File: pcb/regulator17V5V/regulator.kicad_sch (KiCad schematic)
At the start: 8 parts, among them J1 Conn_01x05_Socket, J2 Conn_01x05_Socket, J3 Conn_01x02, U1 TPS82130

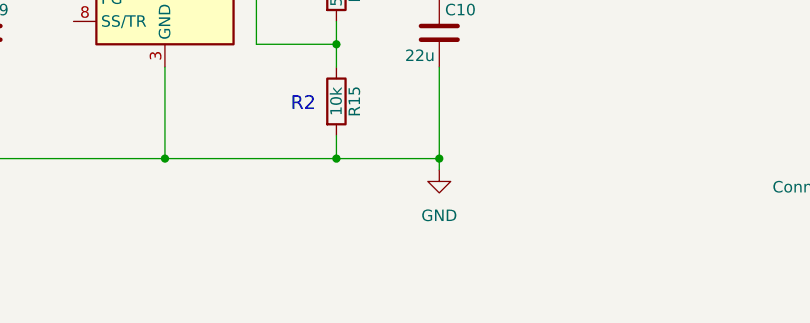
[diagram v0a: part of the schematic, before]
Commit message: Add receiver for IKEA Metod cupboard
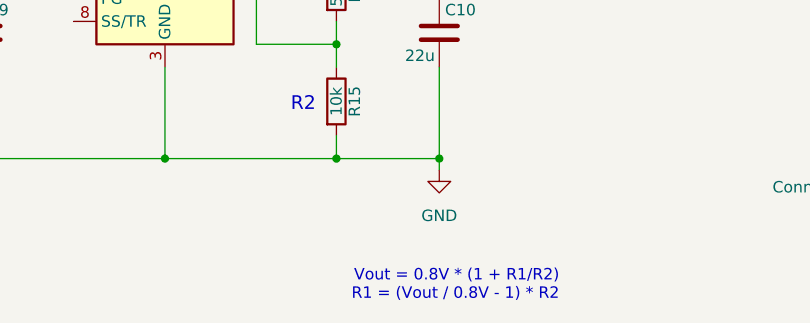
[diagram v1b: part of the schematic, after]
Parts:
- J1, J2: footprint local:Holes -> local:SolderHoles3pin10mm
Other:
- note added: "Vout = 0.8V * (1 + R1/R2) R1 = (Vout / 0.8V - 1) * R2"

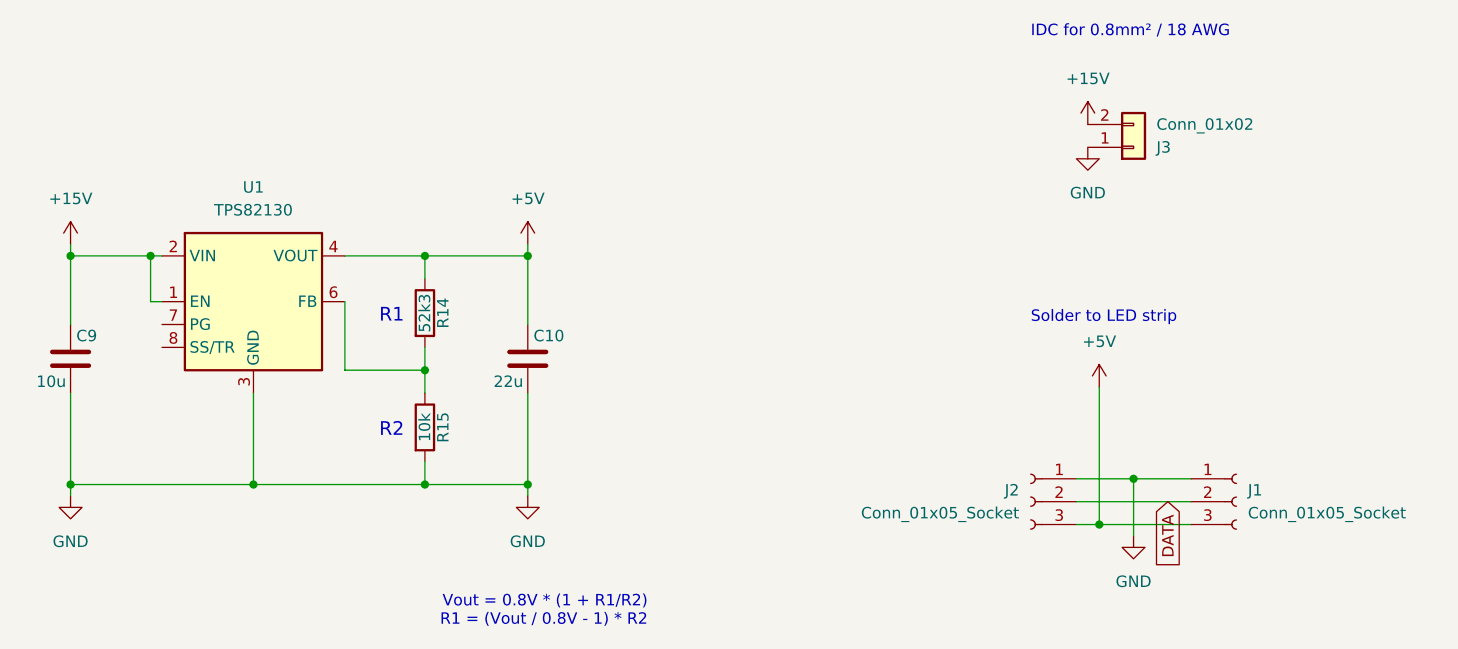
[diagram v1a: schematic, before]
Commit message: Use ISL3280E
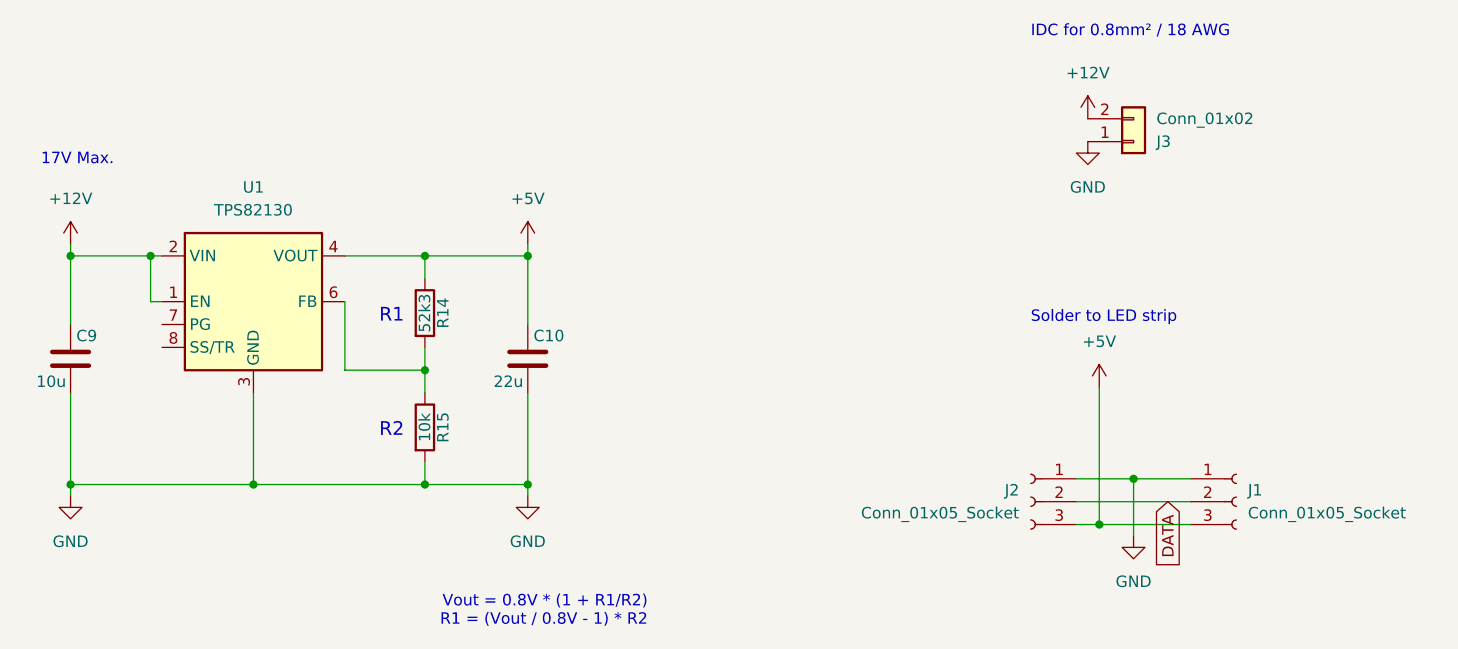
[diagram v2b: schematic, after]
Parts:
- C10: footprint Capacitor_SMD:C_0805_2012Metric -> local:0805
- C9: footprint Capacitor_SMD:C_1206_3216Metric -> local:1206
- R14, R15: footprint Resistor_SMD:R_0603_1608Metric -> local:0603
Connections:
- net +15V renamed +12V
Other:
- note added: "17V Max."
- moved on the sheet: J3
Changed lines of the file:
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@@
+		)
+	)
+	(text "17V Max."
+		(exclude_from_sim no)
+		(at 84.836 70.104 0)
+		(effects
+			(font
+				(size 1.27 1.27)
+			)
+			(justify right bottom)
 		)
 	)
@@
 			)
 		)
-		(property "Footprint" "Capacitor_SMD:C_0805_2012Metric"
+		(property "Footprint" "local:0805"
 			(at 131.7752 95.25 0)
 			(effects
@@
 	)
 	(symbol
+		(lib_id "power:+12V")
+		(at 80.01 78.74 0)
+		(unit 1)
+		(exclude_from_sim no)
+		(in_bom yes)
+		(on_board yes)
+		(dnp no)
+		(fields_autoplaced yes)
+		(property "Reference" "#PWR03"
+			(at 80.01 82.55 0)
+			(effects
+				(font
+					(size 1.27 1.27)
+				)
+				(hide yes)
+			)
+		)
+		(property "Value" "+12V"
+			(at 80.01 73.66 0)
+			(effects
+				(font
+					(size 1.27 1.27)
+				)
+			)
+		)
+		(property "Footprint" ""
+			(at 80.01 78.74 0)
+			(effects
+				(font
+					(size 1.27 1.27)
+				)
+				(hide yes)
+			)
+		)
+		(property "Datasheet" ""
+			(at 80.01 78.74 0)
+			(effects
+				(font
+					(size 1.27 1.27)
+				)
+				(hide yes)
+			)
+		)
+		(property "Description" "Power symbol creates a global label with name \"+12V\""
+			(at 80.01 78.74 0)
+			(effects
+				(font
+					(size 1.27 1.27)
+				)
+				(hide yes)
+			)
+		)
+		(pin "1"
+		)
+		(instances
+			(project ""
+				(path "/69324be2-df3f-4542-80d7-138e50496095"
+					(reference "#PWR03")
+					(unit 1)
+				)
+			)
+		)
+	)
+	(symbol
 		(lib_id "power:+5V")
 		(at 130.81 78.74 0)
@@
 			)
 		)
-		(property "Footprint" "Resistor_SMD:R_0603_1608Metric"
+		(property "Footprint" "local:0603"
 			(at 117.602 86.36 90)
 			(effects
@@
 	)
 	(symbol
+		(lib_id "power:+12V")
+		(at 193.04 64.77 0)
+		(unit 1)
+		(exclude_from_sim no)
+		(in_bom yes)
+		(on_board yes)
+		(dnp no)
+		(fields_autoplaced yes)
+		(property "Reference" "#PWR05"
+			(at 193.04 68.58 0)
+			(effects
+				(font
+					(size 1.27 1.27)
+				)
+				(hide yes)
+			)
+		)
+		(property "Value" "+12V"
+			(at 193.04 59.69 0)
+			(effects
+				(font
+					(size 1.27 1.27)
+				)
+			)
+		)
+		(property "Footprint" ""
+			(at 193.04 64.77 0)
+			(effects
+				(font
+					(size 1.27 1.27)
+				)
+				(hide yes)
+			)
+		)
+		(property "Datasheet" ""
+			(at 193.04 64.77 0)
+			(effects
+				(font
+					(size 1.27 1.27)
+				)
+				(hide yes)
+			)
+		)
+		(property "Description" "Power symbol creates a global label with name \"+12V\""
+			(at 193.04 64.77 0)
+			(effects
+				(font
+					(size 1.27 1.27)
+				)
+				(hide yes)
+			)
+		)
+		(pin "1"
+		)
+		(instances
+			(project "regulator"
+				(path "/69324be2-df3f-4542-80d7-138e50496095"
+					(reference "#PWR05")
+					(unit 1)
+				)
+			)
+		)
+	)
+	(symbol
 		(lib_id "Device:R")
 		(at 119.38 99.06 0)
@@
 			)
 		)
-		(property "Footprint" "Resistor_SMD:R_0603_1608Metric"
+		(property "Footprint" "local:0603"
 			(at 117.602 99.06 90)
 			(effects
@@
 	(symbol
 		(lib_id "Connector_Generic:Conn_01x02")
-		(at 198.12 67.945 0)
+		(at 198.12 67.31 0)
 		(mirror x)
 		(unit 1)
@@
 		(dnp no)
 		(property "Reference" "J3"
-			(at 200.66 67.945 0)
+			(at 200.66 67.31 0)
 			(effects
 				(font
@@
 		)
 		(property "Value" "Conn_01x02"
-			(at 200.66 65.405 0)
+			(at 200.66 64.77 0)
 			(effects
 				(font
@@
 		)
 		(property "Footprint" "local:Kyocera-009176002001906"
-			(at 198.12 67.945 0)
+			(at 198.12 67.31 0)
 			(effects
 				(font
@@
 		)
 		(property "Datasheet" "~"
-			(at 198.12 67.945 0)
-			(effects
-				(font
-					(size 1.27 1.27)
-				)
-				(hide yes)
-			)
-		)
-		(property "Description" ""
-			(at 198.12 67.945 0)
+			(at 198.12 67.31 0)
+			(effects
+				(font
+					(size 1.27 1.27)
+				)
+				(hide yes)
+			)
+		)
+		(property "Description" ""
+			(at 198.12 67.31 0)
 			(effects
 				(font
@@
 	(symbol
 		(lib_id "power:GND")
-		(at 193.04 67.945 0)
+		(at 193.04 67.31 0)
 		(unit 1)
 		(exclude_from_sim no)
@@
 		(dnp no)
 		(property "Reference" "#PWR08"
-			(at 193.04 74.295 0)
+			(at 193.04 73.66 0)
 			(effects
 				(font
@@
 		)
 		(property "Value" "GND"
-			(at 193.04 73.025 0)
+			(at 193.04 72.39 0)
 			(effects
 				(font
@@
 		)
 		(property "Footprint" ""
-			(at 193.04 67.945 0)
+			(at 193.04 67.31 0)
 			(effects
 				(font
@@
 		)
 		(property "Datasheet" ""
-			(at 193.04 67.945 0)
-			(effects
-				(font
-					(size 1.27 1.27)
-				)
-				(hide yes)
-			)
-		)
-		(property "Description" ""
-			(at 193.04 67.945 0)
+			(at 193.04 67.31 0)
+			(effects
+				(font
+					(size 1.27 1.27)
+				)
+				(hide yes)
+			)
+		)
+		(property "Description" ""
+			(at 193.04 67.31 0)
 			(effects
 				(font
@@
 			)
 		)
-		(property "Footprint" "Capacitor_SMD:C_1206_3216Metric"
+		(property "Footprint" "local:1206"
 			(at 80.9752 95.25 0)
 			(effects
@@
 					(unit 1)
 				)
-			)
-		)
-	)
-	(symbol
-		(lib_id "power:+15V")
-		(at 193.04 65.405 0)
-		(unit 1)
-		(exclude_from_sim no)
-		(in_bom yes)
-		(on_board yes)
-		(dnp no)
-		(fields_autoplaced yes)
-		(property "Reference" "#PWR09"
-			(at 193.04 69.215 0)
-			(effects
-				(font
-					(size 1.27 1.27)
-				)
-				(hide yes)
-			)
-		)
-		(property "Value" "+15V"
-			(at 193.04 60.325 0)
-			(effects
-				(font
-					(size 1.27 1.27)
-				)
-			)
-		)
-		(property "Footprint" ""
-			(at 193.04 65.405 0)
-			(effects
-				(font
-					(size 1.27 1.27)
-				)
-				(hide yes)
-			)
-		)
-		(property "Datasheet" ""
-			(at 193.04 65.405 0)
-			(effects
-				(font
-					(size 1.27 1.27)
-				)
-				(hide yes)
-			)
-		)
-		(property "Description" ""
-			(at 193.04 65.405 0)
-			(effects
-				(font
-					(size 1.27 1.27)
-				)
-				(hide yes)
-			)
-		)
-		(pin "1"
-		)
-		(instances
-			(project "regulator"
-				(path "/69324be2-df3f-4542-80d7-138e50496095"
-					(reference "#PWR09")
-					(unit 1)
-				)
-			)
-		)
-	)
-	(symbol
-		(lib_id "power:+15V")
-		(at 80.01 78.74 0)
-		(unit 1)
-		(exclude_from_sim no)
-		(in_bom yes)
-		(on_board yes)
-		(dnp no)
-		(fields_autoplaced yes)
-		(property "Reference" "#PWR05"
-			(at 80.01 82.55 0)
-			(effects
-				(font
-					(size 1.27 1.27)
-				)
-				(hide yes)
-			)
-		)
-		(property "Value" "+15V"
-			(at 80.01 73.66 0)
-			(effects
-				(font
-					(size 1.27 1.27)
-				)
-			)
-		)
-		(property "Footprint" ""
-			(at 80.01 78.74 0)
-			(effects
-				(font
-					(size 1.27 1.27)
-				)
-				(hide yes)
-			)
-		)
-		(property "Datasheet" ""
-			(at 80.01 78.74 0)
-			(effects
-				(font
-					(size 1.27 1.27)
-				)
-				(hide yes)
-			)
-		)
-		(property "Description" ""
-			(at 80.01 78.74 0)
-			(effects
-				(font
-					(size 1.27 1.27)
-				)
-				(hide yes)
-			)
-		)
-		(pin "1"
-		)
-		(instances
-			(project "regulator"
-				(path "/69324be2-df3f-4542-80d7-138e50496095"
-					(reference "#PWR05")
-					(unit 1)
-				)
